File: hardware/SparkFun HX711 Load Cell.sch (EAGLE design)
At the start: 29 parts, among them Q1 MMBT4403, U1 HX711, U7 OSHW-LOGOS

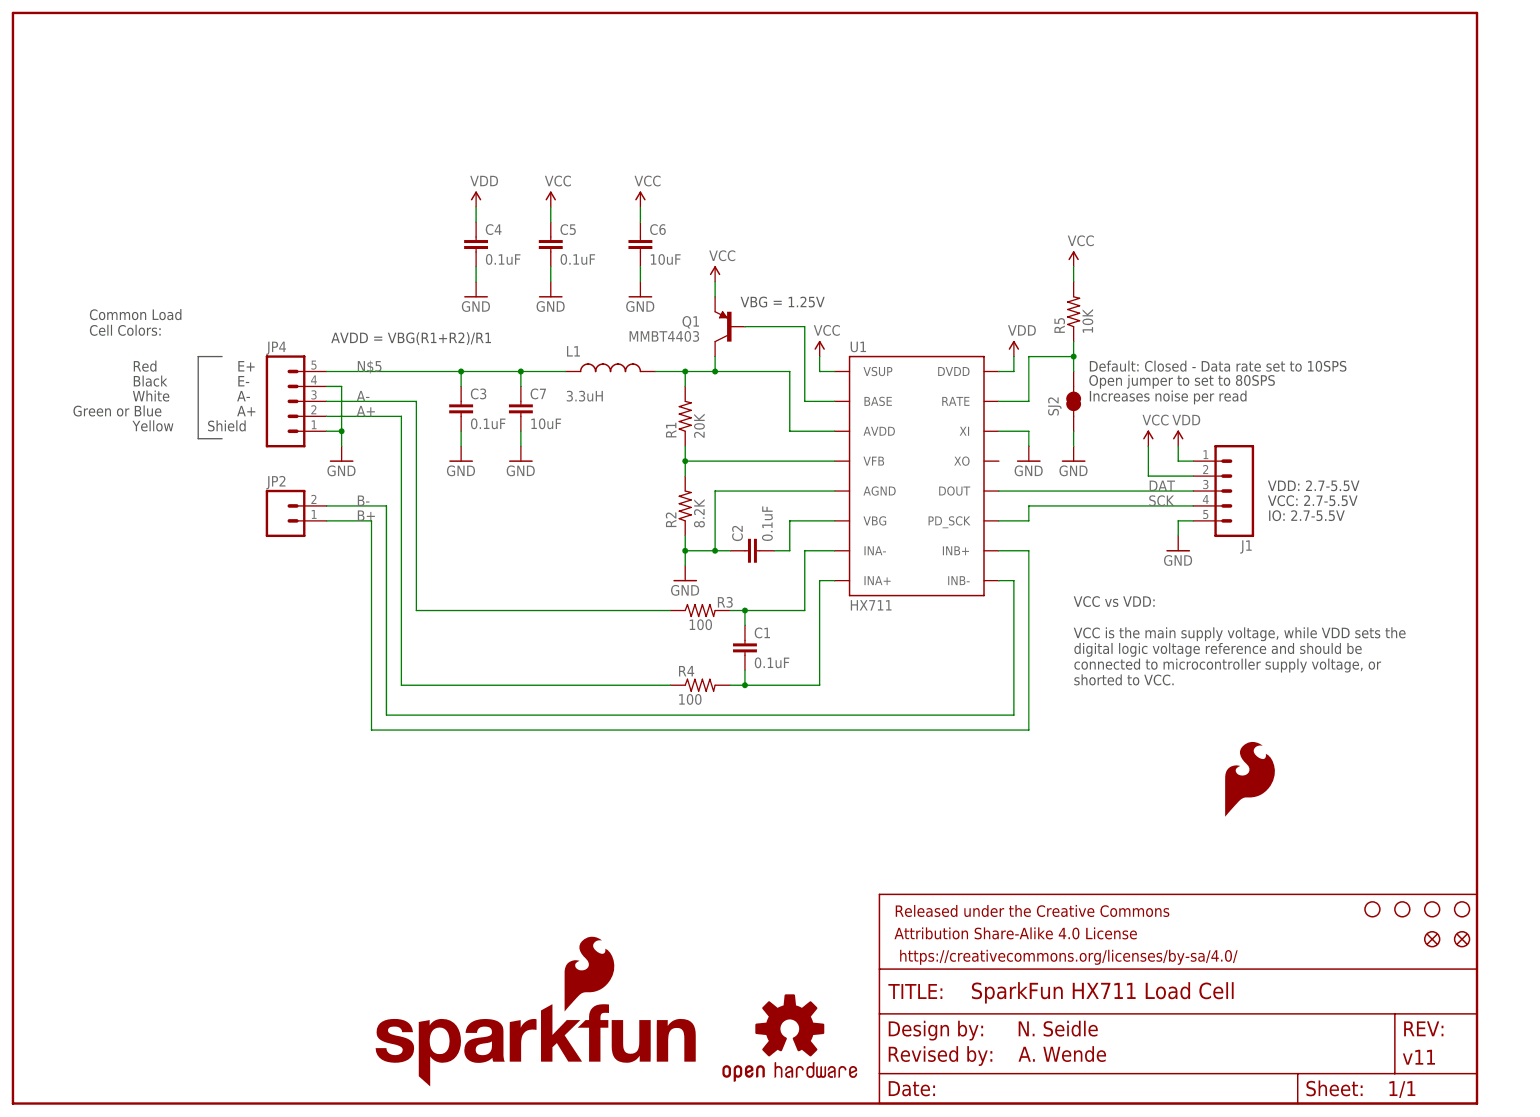
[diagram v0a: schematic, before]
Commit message: Revision 11 (Update)
Corrected net label from N$5 to AVDD.
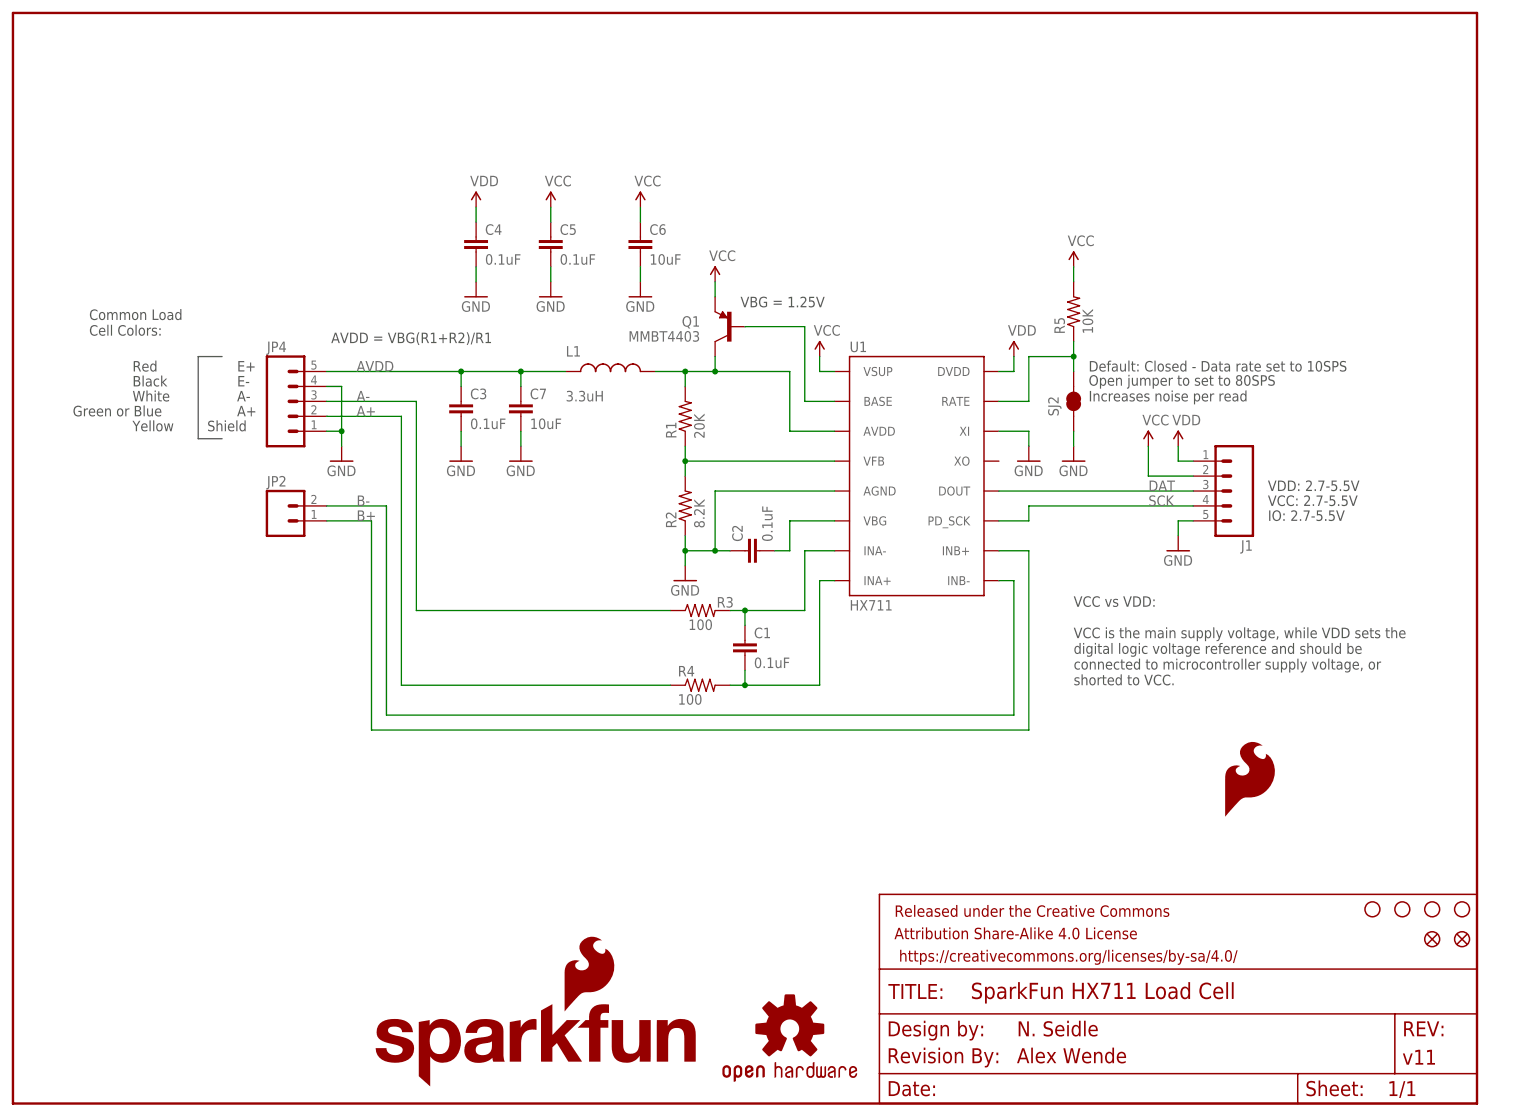
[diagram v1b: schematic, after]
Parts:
- added U$1: REVISION, SparkFun-Aesthetics:REVISION
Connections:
- net AVDD: now also C3.1, C7.1, JP4.5, L1.1; no longer L1.2, Q1.C, R1.2, U1.AVDD
- net N$5: now also L1.2, Q1.C, R1.2, U1.AVDD; no longer C3.1, C7.1, JP4.5, L1.1
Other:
- note added: "Alex Wende"
- note removed: "A. Wende"
- note removed: "Revised by:"
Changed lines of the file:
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@@
 <part name="GND10" library="SparkFun-Aesthetics" deviceset="GND" device=""/>
 <part name="C4" library="SparkFun-Capacitors" deviceset="0.1UF-25V-5%(0603)" device="" value="0.1uF"/>
+<part name="U$1" library="SparkFun-Aesthetics" deviceset="REVISION" device=""/>
 </parts>
 <sheets>
@@
 <wire x1="31.496" y1="127" x2="35.56" y2="127" width="0.2032" layer="97"/>
 <wire x1="31.496" y1="113.03" x2="35.56" y2="113.03" width="0.2032" layer="97"/>
-<text x="148.59" y="7.112" size="2.54" layer="94">Revised by:</text>
-<text x="170.942" y="7.112" size="2.54" layer="94">A. Wende</text>
 <text x="213.36" y="104.14" size="1.778" layer="97">VDD: 2.7-5.5V</text>
 <text x="180.34" y="71.12" size="1.778" layer="97">VCC vs VDD:
@@
 connected to microcontroller supply voltage, or
 shorted to VCC.</text>
+<text x="170.688" y="6.858" size="2.54" layer="94">Alex Wende</text>
 </plain>
 <instances>
@@
 <instance part="GND10" gate="1" x="78.74" y="137.16"/>
 <instance part="C4" gate="G$1" x="78.74" y="144.78"/>
+<instance part="U$1" gate="G$1" x="148.59" y="6.858"/>
 </instances>
 <busses>
@@
 </segment>
 </net>
-<net name="AVDD" class="0">
+<net name="N$5" class="0">
 <segment>
 <pinref part="Q1" gate="G$1" pin="C"/>
@@
 </segment>
 </net>
-<net name="N$5" class="0">
+<net name="AVDD" class="0">
 <segment>
 <pinref part="C7" gate="G$1" pin="1"/>
